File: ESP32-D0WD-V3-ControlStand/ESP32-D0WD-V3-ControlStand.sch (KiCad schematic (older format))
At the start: 40 parts

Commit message: Nearly complete schematic.  Added Antenna footprint.
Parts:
- removed R? (x2): 2.4K Ohms, Resistors_THT:R_Axial_DIN0207_L6.3mm_D2.5mm_P2.54mm_Vertical, symbol R
- removed U?: TTGO-T1, ~, symbol TTGO-T1
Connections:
- net labels removed: MISO, MOSI, SCLK
- wire segments 120 -> 113
- no-connect marks 15 -> 4
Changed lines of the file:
@@
 $Descr USLetter 11000 8500
 encoding utf-8
-Sheet 1 6
+Sheet 1 7
 Title "ESP32-D0WD-V3-ControlStand"
 Date "2022-07-25"
@@
 	5550 1800 5550 1750
 Connection ~ 5250 1800
-$Comp
-L TTGO-T1 U?
-U 1 1 62DF044B
-P 5350 3950
-F 0 "U?" H 5350 3950 60  0000 C CNN
-F 1 "TTGO-T1" H 5350 4500 60  0000 C CNN
-F 2 "~" H 5350 3950 60  0000 C CNN
-F 3 "~" H 5350 3950 60  0000 C CNN
-	1    5350 3950
-	1    0    0    -1
-$EndComp
-$Comp
-L +3.3V-RESCUE-ESP32ControlStand #PWR?
-U 1 1 62DF044C
-P 4900 3400
-F 0 "#PWR?" H 4900 3360 30  0001 C CNN
-F 1 "+3.3V" H 4900 3510 30  0000 C CNN
-F 2 "" H 4900 3400 60  0000 C CNN
-F 3 "" H 4900 3400 60  0000 C CNN
-	1    4900 3400
-	1    0    0    -1
-$EndComp
-$Comp
-L +5V #PWR?
-U 1 1 62DF044D
-P 5900 3800
-F 0 "#PWR?" H 5900 3890 20  0001 C CNN
-F 1 "+5V" H 5900 3890 30  0000 C CNN
-F 2 "" H 5900 3800 60  0000 C CNN
-F 3 "" H 5900 3800 60  0000 C CNN
-	1    5900 3800
-	0    1    1    0
-$EndComp
-$Comp
-L GND-RESCUE-ESP32ControlStand #PWR?
-U 1 1 62DF044E
-P 5900 3500
-F 0 "#PWR?" H 5900 3500 30  0001 C CNN
-F 1 "GND" H 5900 3430 30  0001 C CNN
-F 2 "" H 5900 3500 60  0000 C CNN
-F 3 "" H 5900 3500 60  0000 C CNN
-	1    5900 3500
-	0    -1   -1   0
-$EndComp
-$Comp
-L GND-RESCUE-ESP32ControlStand #PWR?
-U 1 1 62DF044F
-P 4750 4150
-F 0 "#PWR?" H 4750 4150 30  0001 C CNN
-F 1 "GND" H 4750 4080 30  0001 C CNN
-F 2 "" H 4750 4150 60  0000 C CNN
-F 3 "" H 4750 4150 60  0000 C CNN
-	1    4750 4150
-	0    1    1    0
-$EndComp
-Wire Wire Line
-	4900 3500 4900 3400
-Wire Wire Line
-	5900 3500 5800 3500
-Wire Wire Line
-	5900 3800 5800 3800
-Wire Wire Line
-	4750 4150 4900 4150
-Text Label 5800 3950 0    25   ~ 0
+Text Label 4100 3400 2    61   ~ 0
 CAN_TX
-Text Label 5800 4100 0    25   ~ 0
+Text Label 4100 3250 2    61   ~ 0
 CAN_RX
-Text Label 5800 3750 0    25   ~ 0
+Text Label 4100 3650 2    61   ~ 0
 SDA
-Text Label 5800 3600 0    25   ~ 0
+Text Label 4100 3550 2    61   ~ 0
 SCL
-Text Label 5800 4200 0    25   ~ 0
-MISO
-Text Label 5800 4250 0    25   ~ 0
-MOSI
-Text Label 4900 4050 2    25   ~ 0
-SCLK
 Text Label 2600 3700 0    60   ~ 0
 CAN_TX
 Text Label 2600 4000 0    60   ~ 0
 CAN_RX
-Text Label 4900 3550 2    25   ~ 0
+Text Label 4100 4050 2    61   ~ 0
 RST
 Text Label 8000 2250 2    60   ~ 0
@@
 Text Label 8000 3050 2    60   ~ 0
 Brake
-Text Label 4900 3600 2    25   ~ 0
+Text Label 4100 3800 2    61   ~ 0
 Horn
-Text Label 4900 3650 2    25   ~ 0
+Text Label 4100 3900 2    61   ~ 0
 Brake
 Text Label 8100 3850 2    60   ~ 0
@@
 Text Label 8100 4050 2    60   ~ 0
 ThrottleB
-Text Label 5800 3550 0    25   ~ 0
+Text Label 5950 3400 0    61   ~ 0
 ThrottleA
-Text Label 5800 3850 0    25   ~ 0
+Text Label 5950 3500 0    61   ~ 0
 ThrottleB
 $Comp
@@
 Text Label 6750 4700 2    60   ~ 0
 Reverser
-Text Label 4900 4000 2    25   ~ 0
+Text Label 5950 3300 0    61   ~ 0
 Reverser
 Text Label 8000 1100 2    60   ~ 0
@@
 Text Label 3450 1950 0    60   ~ 0
 Status_R
-Text Label 4900 3700 2    25   ~ 0
+Text Label 4100 4400 2    61   ~ 0
 Button_A
-Text Label 4900 3750 2    25   ~ 0
+Text Label 4100 4500 2    61   ~ 0
 Button_B
-Text Label 4900 3850 2    25   ~ 0
+Text Label 4100 4600 2    61   ~ 0
 Button_C
-Text Label 4900 3900 2    25   ~ 0
+Text Label 4100 4700 2    61   ~ 0
 Button_D
-Text Label 4900 3950 2    25   ~ 0
+Text Label 5950 3200 0    61   ~ 0
 Bell
-Text Label 5800 3900 0    25   ~ 0
+Text Label 5950 3650 0    61   ~ 0
 L_Off
-Text Label 5800 4000 0    25   ~ 0
+Text Label 5950 3750 0    61   ~ 0
 L_Dim
-Text Label 5800 4050 0    25   ~ 0
+Text Label 5950 3850 0    61   ~ 0
 L_Bright
-Text Label 5800 4150 0    25   ~ 0
+Text Label 5950 3950 0    61   ~ 0
 L_Ditch
-Text Label 4900 4100 2    25   ~ 0
+Text Label 4100 4300 2    61   ~ 0
 Status_R
-Text Label 4900 3800 2    25   ~ 0
+Text Label 4100 4200 2    61   ~ 0
 Status_G
 NoConn ~ 5650 1750
 NoConn ~ 5450 1750
 NoConn ~ 5150 1750
-NoConn ~ 4900 4250
-NoConn ~ 4900 4300
-NoConn ~ 4900 4350
-NoConn ~ 5800 4350
-NoConn ~ 5800 4300
-NoConn ~ 5800 3650
-NoConn ~ 4900 4050
-NoConn ~ 5800 4200
-NoConn ~ 5800 4250
-NoConn ~ 5800 3700
 $Comp
 L BARREL_JACK CON?
@@
 	5400 2100 5400 1800
 Connection ~ 5400 1800
-NoConn ~ 4900 4200
-$Comp
-L R R?
-U 1 1 62DF0459
-P 6200 3600
-F 0 "R?" V 6280 3600 50  0000 C CNN
-F 1 "2.4K Ohms" V 6200 3600 50  0000 C CNN
-F 2 "Resistors_THT:R_Axial_DIN0207_L6.3mm_D2.5mm_P2.54mm_Vertical" V 6130 3600 50  0001 C CNN
-F 3 "" H 6200 3600 50  0001 C CNN
-	1    6200 3600
-	0    1    1    0
-$EndComp
-$Comp
-L R R?
-U 1 1 62DF045A
-P 6200 3750
-F 0 "R?" V 6280 3750 50  0000 C CNN
-F 1 "2.4K Ohms" V 6200 3750 50  0000 C CNN
-F 2 "Resistors_THT:R_Axial_DIN0207_L6.3mm_D2.5mm_P2.54mm_Vertical" V 6130 3750 50  0001 C CNN
-F 3 "" H 6200 3750 50  0001 C CNN
-	1    6200 3750
-	0    1    1    0
-$EndComp
-Wire Wire Line
-	6050 3600 5800 3600
-Wire Wire Line
-	6050 3750 5800 3750
-Wire Wire Line
-	6350 3500 6350 3750
-$Comp
-L +3.3V-RESCUE-ESP32ControlStand #PWR?
-U 1 1 62DF045B
-P 6350 3500
-F 0 "#PWR?" H 6350 3460 30  0001 C CNN
-F 1 "+3.3V" H 6350 3610 30  0000 C CNN
-F 2 "" H 6350 3500 60  0000 C CNN
-F 3 "" H 6350 3500 60  0000 C CNN
-	1    6350 3500
-	1    0    0    -1
-$EndComp
-Connection ~ 6350 3600
 $Sheet
 S 4100 3100 1850 1800
@@
 F0 "Processor Section" 60
 F1 "ProcessorSection.sch" 60
+F2 "CAN_RX" I L 4100 3250 60
+F3 "SCL" I L 4100 3550 60
+F4 "SDA" B L 4100 3650 60
+F5 "CAN_TX" O L 4100 3400 60
+F6 "VP" I L 4100 3800 60
+F7 "VN" I L 4100 3900 60
+F8 "Reset" B L 4100 4050 60
+F9 "32" O L 4100 4200 60
+F10 "12" O L 4100 4300 60
+F11 "33" I L 4100 4600 60
+F12 "34" I L 4100 4400 60
+F13 "35" I L 4100 4500 60
+F14 "25" I L 4100 4700 60
+F15 "26" I R 5950 3200 60
+F16 "27" I R 5950 3300 60
+F17 "23" I R 5950 3400 60
+F18 "19" I R 5950 3500 60
+F19 "18" I R 5950 3650 60
+F20 "17" I R 5950 3750 60
+F21 "16" I R 5950 3850 60
+F22 "0" I R 5950 3950 60
 $EndSheet
 $EndSCHEMATC

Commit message: Conversion to SMD continues...
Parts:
- removed J?: I2C Display, ~, symbol CONN_6
- removed MOD?: I2C_DISPLAY, ~, symbol I2C_Display
- removed P?: CONN_6, ~, symbol CONN_6
- added J?: STEMMA (Display), Connectors_JST:JST_PH_S4B-PH-SM4-TB_04x2.00mm_Angled, symbol Conn_01x04
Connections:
- wire segments 113 -> 108
- no-connect marks 4 -> 3
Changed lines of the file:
@@
 $Descr USLetter 11000 8500
 encoding utf-8
-Sheet 1 7
+Sheet 1 6
 Title "ESP32-D0WD-V3-ControlStand"
 Date "2022-07-25"
@@
 $EndComp
 $Comp
-L CONN_6 J?
-U 1 1 62DF0425
-P 8350 5450
-F 0 "J?" V 8300 5450 50  0000 C CNN
-F 1 "I2C Display" V 8400 5450 50  0000 C CNN
-F 2 "~" H 8350 5450 60  0000 C CNN
-F 3 "~" H 8350 5450 60  0000 C CNN
-	1    8350 5450
-	1    0    0    -1
-$EndComp
-$Comp
 L CONN_5 J?
 U 1 1 62DF0426
@@
 F1 "ButtonLedPanel1.sch" 50
 $EndSheet
-$Comp
-L CONN_6 P?
-U 1 1 62DF042A
-P 8950 5450
-F 0 "P?" V 8900 5450 50  0000 C CNN
-F 1 "CONN_6" V 9000 5450 50  0000 C CNN
-F 2 "~" H 8950 5450 60  0000 C CNN
-F 3 "~" H 8950 5450 60  0000 C CNN
-	1    8950 5450
-	-1   0    0    -1
-$EndComp
-$Comp
-L I2C_Display MOD?
-U 1 1 62DF042B
-P 9900 5450
-F 0 "MOD?" H 10050 5650 60  0000 C CNN
-F 1 "I2C_DISPLAY" H 10000 5350 60  0000 C CNN
-F 2 "~" H 9900 5450 60  0000 C CNN
-F 3 "~" H 9900 5450 60  0000 C CNN
-	1    9900 5450
-	1    0    0    -1
-$EndComp
-Wire Wire Line
-	9550 5200 9300 5200
-Wire Wire Line
-	9550 5300 9300 5300
-Wire Wire Line
-	9550 5400 9300 5400
-Wire Wire Line
-	9550 5500 9300 5500
-Wire Wire Line
-	9550 5600 9300 5600
-Wire Wire Line
-	9550 5700 9300 5700
 Text Label 3550 5900 2    60   ~ 0
 SCL
 Text Label 3550 6000 2    60   ~ 0
 SDA
-Text Label 8000 5400 2    60   ~ 0
+Text Label 8050 6100 2    60   ~ 0
 GND
-Text Label 8000 5500 2    60   ~ 0
-RST
-Text Label 8000 5600 2    60   ~ 0
+Text Label 8050 6400 2    60   ~ 0
 SCL
-Text Label 8000 5700 2    60   ~ 0
+Text Label 8050 6300 2    60   ~ 0
 SDA
-NoConn ~ 8000 5300
 $Comp
 L GND-RESCUE-ESP32ControlStand #PWR?
@@
 L +5V #PWR?
 U 1 1 62DF0440
-P 8000 5100
-F 0 "#PWR?" H 8000 5190 20  0001 C CNN
-F 1 "+5V" H 8000 5190 30  0000 C CNN
-F 2 "" H 8000 5100 60  0000 C CNN
-F 3 "" H 8000 5100 60  0000 C CNN
-	1    8000 5100
+P 7750 6050
+F 0 "#PWR?" H 7750 6140 20  0001 C CNN
+F 1 "+5V" H 7750 6140 30  0000 C CNN
+F 2 "" H 7750 6050 60  0000 C CNN
+F 3 "" H 7750 6050 60  0000 C CNN
+	1    7750 6050
 	1    0    0    -1
 $EndComp
@@
 	1    0    0    -1
 $EndComp
-Wire Wire Line
-	8000 5100 8000 5200
 Wire Wire Line
 	3550 5500 3550 5600
@@
 F22 "0" I R 5950 3950 60
 $EndSheet
+$Comp
+L Conn_01x04 J?
+U 1 1 62E14860
+P 8250 6200
+F 0 "J?" H 8250 6400 50  0000 C CNN
+F 1 "STEMMA (Display)" H 8250 5900 50  0000 C CNN
+F 2 "Connectors_JST:JST_PH_S4B-PH-SM4-TB_04x2.00mm_Angled" H 8250 6200 50  0001 C CNN
+F 3 "" H 8250 6200 50  0001 C CNN
+F 4 "JST" H 8250 6200 60  0001 C CNN "Manufacturer_Name"
+F 5 "S4B-PH-SM4-TB" H 8250 6200 60  0001 C CNN "Manufacturer_Part_Number"
+	1    8250 6200
+	1    0    0    -1
+$EndComp
+Wire Wire Line
+	7750 6050 7750 6200
+Wire Wire Line
+	7750 6200 8050 6200
 $EndSCHEMATC

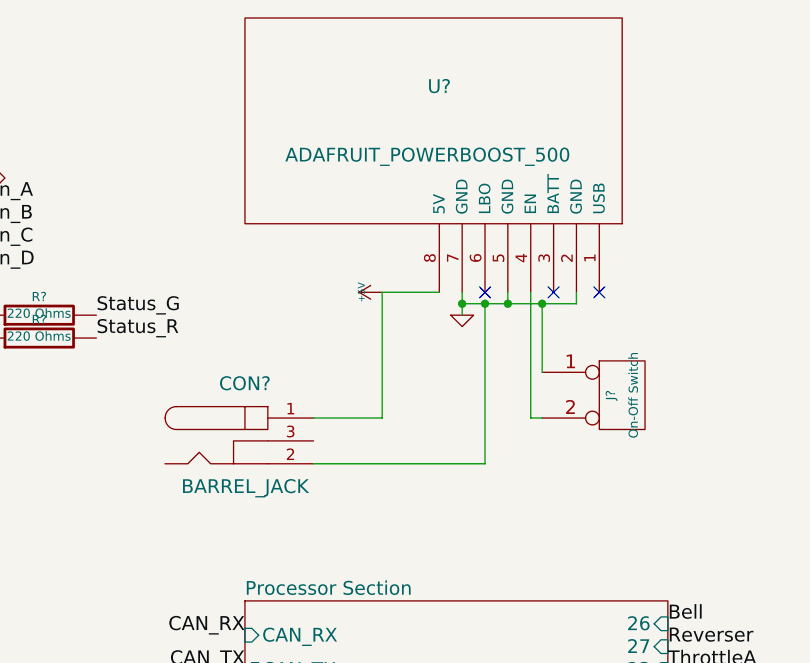
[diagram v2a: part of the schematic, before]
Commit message: Complete PS, work on parts spec.
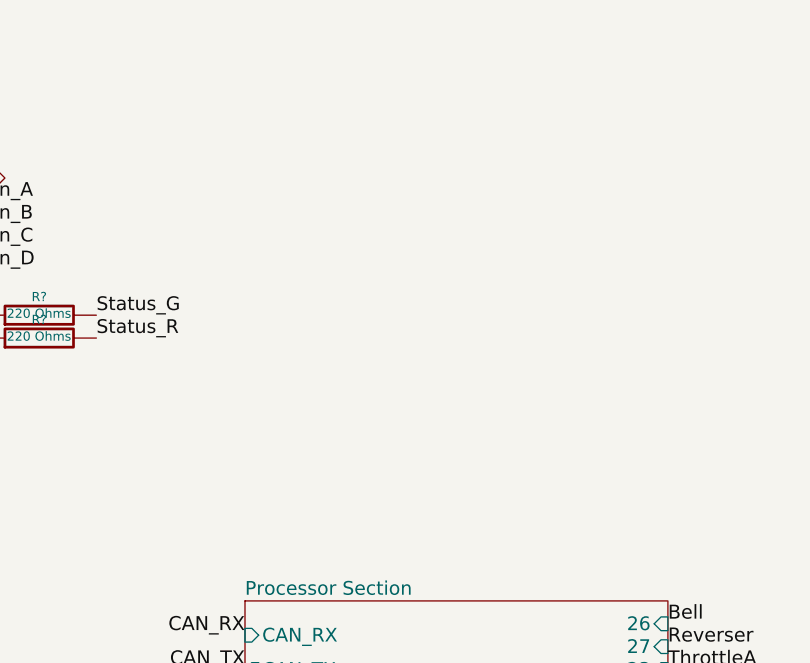
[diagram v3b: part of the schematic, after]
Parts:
- removed CON?: BARREL_JACK, ~, symbol BARREL_JACK
- removed J?: On-Off Switch, ~, symbol CONN_2
- removed U?: ADAFRUIT_POWERBOOST_500, ~, symbol ADAFRUIT_POWERBOOST_500
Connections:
- no-connect marks 3 -> 0
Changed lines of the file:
@@
 LIBS:ESP32-D0WD-V3
 LIBS:W25Q32JVSSIQ
+LIBS:mcp73871
+LIBS:lm2574n-5
 LIBS:ESP32-D0WD-V3-ControlStand-cache
 EELAYER 25 0
@@
 Wire Wire Line
 	3550 5800 3350 5800
-$Comp
-L ADAFRUIT_POWERBOOST_500 U?
-U 1 1 62DF0448
-P 4950 1000
-F 0 "U?" H 4950 850 60  0000 C CNN
-F 1 "ADAFRUIT_POWERBOOST_500" H 5000 1150 60  0000 C CNN
-F 2 "~" H 4950 1000 60  0000 C CNN
-F 3 "~" H 4950 1000 60  0000 C CNN
-	1    4950 1000
-	-1   0    0    1
-$EndComp
-$Comp
-L +5V #PWR?
-U 1 1 62DF0449
-P 4700 1750
-F 0 "#PWR?" H 4700 1840 20  0001 C CNN
-F 1 "+5V" H 4700 1840 30  0000 C CNN
-F 2 "" H 4700 1750 60  0000 C CNN
-F 3 "" H 4700 1750 60  0000 C CNN
-	1    4700 1750
-	0    -1   -1   0
-$EndComp
-$Comp
-L GND-RESCUE-ESP32ControlStand #PWR?
-U 1 1 62DF044A
-P 5050 1850
-F 0 "#PWR?" H 5050 1850 30  0001 C CNN
-F 1 "GND" H 5050 1780 30  0001 C CNN
-F 2 "" H 5050 1850 60  0000 C CNN
-F 3 "" H 5050 1850 60  0000 C CNN
-	1    5050 1850
-	1    0    0    -1
-$EndComp
-Wire Wire Line
-	4700 1750 4950 1750
-Wire Wire Line
-	5050 1750 5050 1850
-Wire Wire Line
-	5250 1750 5250 1800
-Wire Wire Line
-	5050 1800 5550 1800
-Connection ~ 5050 1800
-Wire Wire Line
-	5550 1800 5550 1750
-Connection ~ 5250 1800
 Text Label 4100 3400 2    61   ~ 0
 CAN_TX
@@
 Text Label 4100 4200 2    61   ~ 0
 Status_G
-NoConn ~ 5650 1750
-NoConn ~ 5450 1750
-NoConn ~ 5150 1750
-$Comp
-L BARREL_JACK CON?
-U 1 1 62DF0456
-P 4100 2400
-F 0 "CON?" H 4100 2650 60  0000 C CNN
-F 1 "BARREL_JACK" H 4100 2200 60  0000 C CNN
-F 2 "~" H 4100 2400 60  0000 C CNN
-F 3 "~" H 4100 2400 60  0000 C CNN
-	1    4100 2400
-	1    0    0    -1
-$EndComp
-Wire Wire Line
-	4400 2300 4700 2300
-Wire Wire Line
-	4700 2300 4700 1750
-Wire Wire Line
-	4400 2500 5150 2500
-Wire Wire Line
-	5150 2500 5150 1800
-Connection ~ 5150 1800
 $Comp
 L GND-RESCUE-ESP32ControlStand #PWR?
@@
 	1550 1100 1550 900
 Connection ~ 1550 900
-$Comp
-L CONN_2 J?
-U 1 1 62DF0458
-P 5750 2200
-F 0 "J?" V 5700 2200 40  0000 C CNN
-F 1 "On-Off Switch" V 5800 2200 40  0000 C CNN
-F 2 "~" H 5750 2200 60  0000 C CNN
-F 3 "~" H 5750 2200 60  0000 C CNN
-	1    5750 2200
-	1    0    0    -1
-$EndComp
-Wire Wire Line
-	5350 1750 5350 2300
-Wire Wire Line
-	5350 2300 5400 2300
-Wire Wire Line
-	5400 2100 5400 1800
-Connection ~ 5400 1800
 $Sheet
 S 4100 3100 1850 1800

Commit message: Completed parts spec for ESP32-D0WD-V3-ControlStand.
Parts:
- D1: renamed from D?; footprint ~ -> APHB1608CGKSURKC:APHB1608CGKSURKC; symbol BI_LED -> LED_Dual_ACAC; Mouser Part Number (none) -> 604-APHB1608CGKSURKC
- EN1: renamed from EN?; footprint ~ -> Encoders:Series25L-Encoder
- EN2: renamed from EN?; footprint ~ -> Encoders:ALPSEC12C
- J1, J2, J6: renamed from J?; footprint ~ -> Pin_Headers:Pin_Header_Straight_1x05_Pitch2.54mm; Mouser Part Number (none) -> 523-G800W303018EU
- J4, J5, J7, J8: renamed from J?; footprint ~ -> Pin_Headers:Pin_Header_Straight_1x03_Pitch2.54mm; Mouser Part Number (none) -> 649-1012937890301BLF
- P1: renamed from P?; footprint ~ -> Pin_Headers:Pin_Header_Angled_1x08_Pitch2.54mm; Mouser Part Number (none) -> 649-1012937990801BLF
- P2: renamed from P?; footprint ~ -> Pin_Headers:Pin_Header_Straight_1x08_Pitch2.54mm; Mouser Part Number (none) -> 649-1012937890801BLF
- P3, P4, P5: renamed from P?; footprint ~ -> (none)
- P6, P7: renamed from P?; footprint ~ -> Pin_Headers:Pin_Header_Angled_1x03_Pitch2.54mm; Mouser Part Number (none) -> 855-M20-9750346
- R1, R2: renamed from R?; footprint ~ -> Resistors_SMD:R_0603; Mouser Part Number (none) -> 603-AC0603FR-07220RL
- R3, R4, R5, R6: renamed from R?; footprint ~ -> Resistors_SMD:R_0402; Mouser Part Number (none) -> 279-CRGCQ0402J100K
- RV1, RV2: renamed from RV?; footprint ~ -> (none)
- SW1, SW3, SW4, SW5: renamed from SW?; footprint ~ -> Buttons_Switches_SMD:SW_SPST_EVQQ2; Mouser Part Number (none) -> 667-EVQ-Q2U02W
- SW2: renamed from SW?; footprint ~ -> Buttons_Switches_SMD:SW_SPST_EVQQ2; Mouser part Number (none) -> 667-EVQ-Q2U02W
- SW6: renamed from SW?; footprint ~ -> (none)
- gave numbers to parts that had none: 1
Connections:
- net GND: now also D1.4 (K2)
- net at D1.1 (A1): now also P1.7 (P7); no longer P1.8 (P8)
- net at D1.3 (A2): now also P1.8 (P8); no longer P1.7 (P7)

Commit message: Working on the PCB Layout.
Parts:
- added FD1, FD2, FD3: FidMark, Fiducials:Fiducial_1mm_Dia_2.54mm_Outer_CopperBottom, symbol Mounting_Hole
- added MK1, MK2, MK21, MK22, MK23, MK24, MK3, MK4, MK5, MK6, MK7, MK8: Mounting_Hole, Mounting_Holes:MountingHole_2.5mm, symbol Mounting_Hole
- J3: footprint Connectors_JST:JST_PH_S4B-PH-SM4-TB_04x2.00mm_Angled -> Connectors_JST:JST_PH_B4B-PH-SM4-TB_04x2.00mm_Straight; Manufacturer_Part_Number S4B-PH-SM4-TB -> B4B-PH-SM4-TB
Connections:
- net ThrottleA: now also J8.3 (P3); no longer J8.1 (P1)
- net ThrottleB: now also J8.1 (P1); no longer J8.3 (P3)
- net at EN2.1 (A): now also P7.3 (P3); no longer P7.1 (P1)
- net at EN2.3 (B): now also P7.1 (P1); no longer P7.3 (P3)
- net at EN1.1 (A): now also P6.3 (P3); no longer P6.1 (P1)
- net at EN1.3 (B): now also P6.1 (P1); no longer P6.3 (P3)
- net at J7.1 (P1): now also R6.2; no longer R5.2
- net at J7.3 (P3): now also R5.2; no longer R6.2

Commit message: Completed V0.0 PCB.
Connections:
- net +3.3V renamed +3V3
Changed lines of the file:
@@
 SDA
 $Comp
-L GND-RESCUE-ESP32ControlStand #PWR01
+L GND #PWR01
 U 1 1 62DF042C
 P 7850 1300
@@
 $EndComp
 $Comp
-L +3.3V-RESCUE-ESP32ControlStand #PWR02
+L +3.3V #PWR02
 U 1 1 62DF042D
 P 8000 2000
@@
 $EndComp
 $Comp
-L +3.3V-RESCUE-ESP32ControlStand #PWR03
+L +3.3V #PWR03
 U 1 1 62DF042E
 P 8000 2850
@@
 $EndComp
 $Comp
-L GND-RESCUE-ESP32ControlStand #PWR04
+L GND #PWR04
 U 1 1 62DF042F
 P 8000 2450
@@
 $EndComp
 $Comp
-L GND-RESCUE-ESP32ControlStand #PWR05
+L GND #PWR05
 U 1 1 62DF0430
 P 8000 3250
@@
 $EndComp
 $Comp
-L GND-RESCUE-ESP32ControlStand #PWR06
+L GND #PWR06
 U 1 1 62DF0431
 P 7950 3950
@@
 $EndComp
 $Comp
-L GND-RESCUE-ESP32ControlStand #PWR07
+L GND #PWR07
 U 1 1 62DF043A
 P 3000 1250
@@
 $EndComp
 $Comp
-L +3.3V-RESCUE-ESP32ControlStand #PWR011
+L +3.3V #PWR011
 U 1 1 62DF0444
 P 3900 6650
@@
 $EndComp
 $Comp
-L GND-RESCUE-ESP32ControlStand #PWR012
+L GND #PWR012
 U 1 1 62DF0445
 P 3950 6750
@@
 $EndComp
 $Comp
-L GND-RESCUE-ESP32ControlStand #PWR013
+L GND #PWR013
 U 1 1 62DF0446
 P 3350 5800
@@
 $EndComp
 $Comp
-L +3.3V-RESCUE-ESP32ControlStand #PWR014
+L +3.3V #PWR014
 U 1 1 62DF0447
 P 3400 5650
@@
 $EndComp
 $Comp
-L +3.3V-RESCUE-ESP32ControlStand #PWR015
+L +3.3V #PWR015
 U 1 1 62DF0454
 P 7550 4350
@@
 $EndComp
 $Comp
-L GND-RESCUE-ESP32ControlStand #PWR016
+L GND #PWR016
 U 1 1 62DF0455
 P 6750 5300
@@
 Status_G
 $Comp
-L GND-RESCUE-ESP32ControlStand #PWR017
+L GND #PWR017
 U 1 1 62DF0457
 P 1550 1100

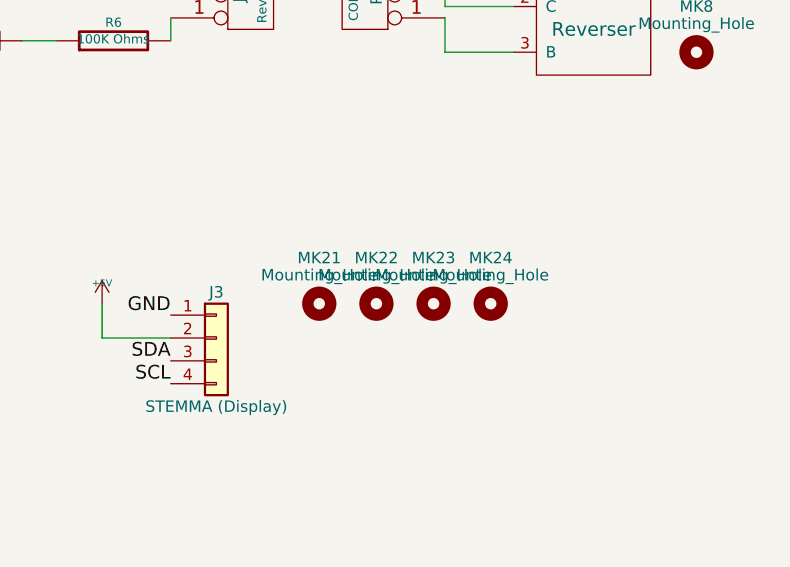
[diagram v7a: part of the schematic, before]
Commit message: Completed V0-1 board (still need to add a few things -- logos and such and adjust silk).
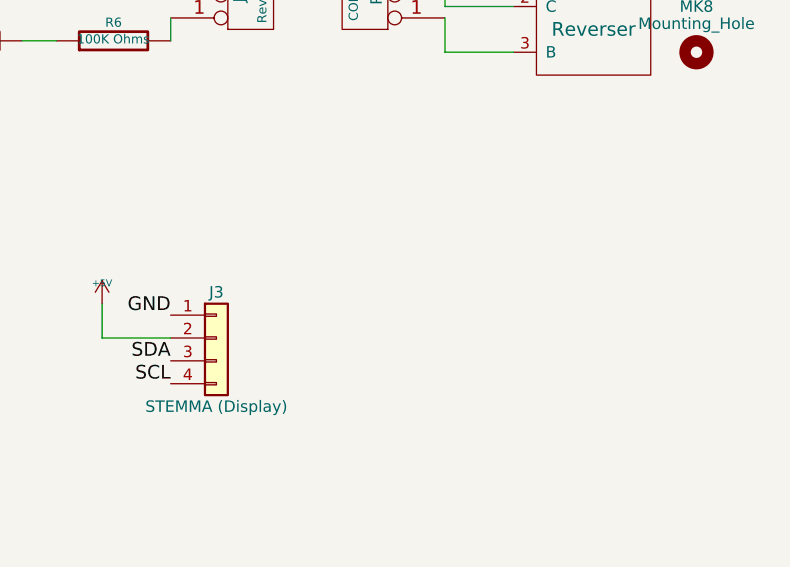
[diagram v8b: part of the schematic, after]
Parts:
- removed MK21, MK22, MK23, MK24: Mounting_Hole, Mounting_Holes:MountingHole_2.5mm, symbol Mounting_Hole
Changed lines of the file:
@@
-	1    0    0    -1
-$EndComp
-$Comp
-L Mounting_Hole MK21
-U 1 1 62E7A85B
-P 8700 6050
-F 0 "MK21" H 8700 6250 50  0000 C CNN
-F 1 "Mounting_Hole" H 8700 6175 50  0000 C CNN
-F 2 "Mounting_Holes:MountingHole_2.5mm" H 8700 6050 50  0001 C CNN
-F 3 "" H 8700 6050 50  0001 C CNN
-	1    8700 6050
-	1    0    0    -1
-$EndComp
-$Comp
-L Mounting_Hole MK22
-U 1 1 62E7A95E
-P 8950 6050
-F 0 "MK22" H 8950 6250 50  0000 C CNN
-F 1 "Mounting_Hole" H 8950 6175 50  0000 C CNN
-F 2 "Mounting_Holes:MountingHole_2.5mm" H 8950 6050 50  0001 C CNN
-F 3 "" H 8950 6050 50  0001 C CNN
-	1    8950 6050
-	1    0    0    -1
-$EndComp
-$Comp
-L Mounting_Hole MK23
-U 1 1 62E7AA57
-P 9200 6050
-F 0 "MK23" H 9200 6250 50  0000 C CNN
-F 1 "Mounting_Hole" H 9200 6175 50  0000 C CNN
-F 2 "Mounting_Holes:MountingHole_2.5mm" H 9200 6050 50  0001 C CNN
-F 3 "" H 9200 6050 50  0001 C CNN
-	1    9200 6050
-	1    0    0    -1
-$EndComp
-$Comp
-L Mounting_Hole MK24
-U 1 1 62E7AB60
-P 9450 6050
-F 0 "MK24" H 9450 6250 50  0000 C CNN
-F 1 "Mounting_Hole" H 9450 6175 50  0000 C CNN
-F 2 "Mounting_Holes:MountingHole_2.5mm" H 9450 6050 50  0001 C CNN
-F 3 "" H 9450 6050 50  0001 C CNN
-	1    9450 6050
 	1    0    0    -1
 $EndComp
